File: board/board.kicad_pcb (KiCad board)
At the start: 4 copper layers, 45 x 13 mm, 36 parts, among them J1 008_USB_2x2, J2 009_1000BASE-T_2x5, U1 LAN9500(A), U2 93AA56AT-I/OT, U3 TC1017-xCT, Y1 25MhZ

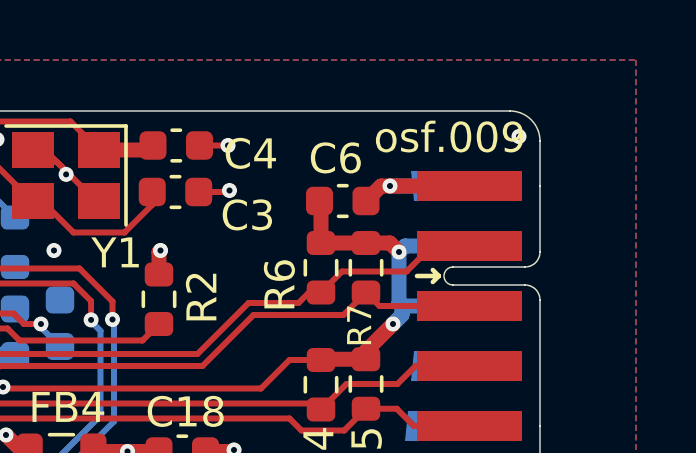
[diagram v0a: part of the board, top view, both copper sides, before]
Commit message: changed osf.009 to osf.019 on silkscreen
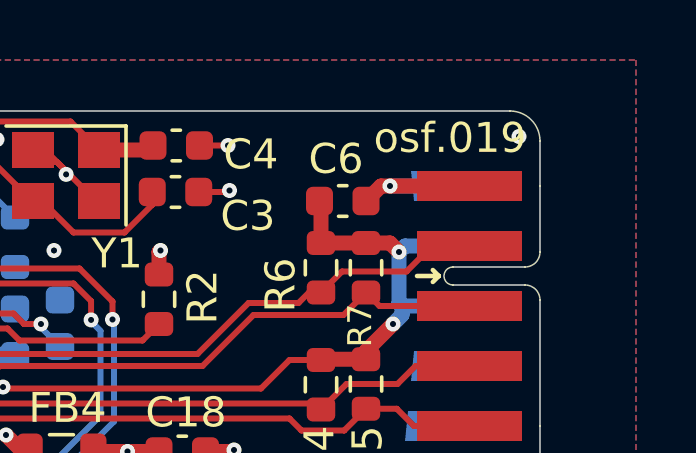
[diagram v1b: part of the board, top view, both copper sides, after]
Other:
- board text added: "osf.019"
- board text removed: "osf.009"
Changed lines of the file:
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@@
   (gr_line (start 131 100) (end 174 100) (layer "Edge.Cuts") (width 0.05))
   (gr_line (start 175 102.5) (end 175 101) (layer "Edge.Cuts") (width 0.05))
-  (gr_text "osf.009" (at 172 100.9) (layer "F.SilkS")
+  (gr_text "osf.019" (at 172 100.9) (layer "F.SilkS")
     (effects (font (size 1 1) (thickness 0.15)))
   )
